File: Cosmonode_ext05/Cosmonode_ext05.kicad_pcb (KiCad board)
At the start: 2 copper layers, 25.4 x 34.3 mm, 16 parts, among them J1 CH340G, J2 GS2, J3 USB_OTG, J4 CONN_01X08, J5 CONN_01X08, J6 CONN_02X05, J7 CONN_01X09, Y1 Crystal_GND2

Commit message: big push!
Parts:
- added J8: Aloes_Logo, Aloes:Aloes_mini, F.Cu at (149.2, 119.4)
- C1, C2: footprint Capacitors_SMD:C_0402_NoSilk -> Capacitors_SMD:C_0603_HandSoldering
- J2: value GS2 -> OSWH_Logo; footprint Connectors:GS2 -> Symbols:OSHW-Logo_5.7x6mm_SilkScreen; moved to B.Cu
- R1, R2, R3, R4: footprint Resistors_SMD:R_0402_NoSilk -> Resistors_SMD:R_0603_HandSoldering
- moved J2 19.8 mm to (153.7, 102.2), turned to 270 degrees
- moved Y1 9.69 mm to (166.4, 109.2), turned to 90 degrees
- moved C1 4.49 mm to (165.7, 101.0), turned to 180 degrees
- moved R2 4.07 mm to (160.0, 104.1)
- moved J6 3.17 mm to (165.1, 118.1)
- moved C2 1.91 mm to (165.7, 104.1), turned to 180 degrees
- moved R1 1.91 mm to (160.0, 101.0)
- moved U1 1.42 mm to (158.8, 110.5)
- moved R3 0.64 mm to (154.3, 104.1), turned to 180 degrees
- moved R4 0.64 mm to (154.3, 101.0)
- moved J3 0.64 mm to (148.6, 110.5)
- renumbered J1 to U1
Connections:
- J7 pad 9: /DTR_1 -> /AREF
- U1 pad 13: /DTR_2 -> Net-(J1-Pad13)
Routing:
- net VCC: track 0.00 -> 69.2 mm
- net /RST: track 0.00 -> 27.1 mm
- net Net-(J1-Pad8): track 0.00 -> 22.7 mm
- net /RX: track 0.00 -> 20.5 mm, vias 0 -> 1
- net /MISO: track 0.00 -> 18.3 mm
- net /TX: track 0.00 -> 17.7 mm
- net Net-(J1-Pad7): track 0.00 -> 16.6 mm
- net /SCK: track 0.00 -> 14.8 mm
- net Net-(J3-Pad6): track 0.00 -> 13.2 mm
- net Net-(C1-Pad1): track 0.00 -> 12.1 mm, vias 0 -> 2
- net GND: track 0.00 -> 11.9 mm, vias 0 -> 6
- net /MOSI: track 0.00 -> 11.8 mm
- net Net-(J1-Pad2): track 0.00 -> 9.70 mm, vias 0 -> 2
- net /USB_N: track 0.00 -> 9.32 mm
- net /USB_P: track 0.00 -> 8.92 mm
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- added copper zone on B.Cu, net GND
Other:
- board text added: "ALOES.IO"

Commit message: big push2
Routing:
- added copper zone on F.Cu, net GND
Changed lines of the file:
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@@
     (links 43)
     (no_connects 0)
-    (area 144.165 85.565 192 130.763333)
+    (area 146.609999 93.904999 172.160001 128.345001)
     (thickness 1.6)
     (drawings 31)
@@
     (trace_clearance 0.2)
     (zone_clearance 0.508)
-    (zone_45_only no)
+    (zone_45_only yes)
     (trace_min 0.2)
     (segment_width 0.2)
@@
     (tags "Micro-USB SMD Typ-B")
     (attr smd)
-    (fp_text reference J3 (at 0 -4 270) (layer F.SilkS)
+    (fp_text reference J3 (at 0 -1.27 270) (layer F.SilkS)
       (effects (font (size 1 1) (thickness 0.15)))
     )
@@
     (fp_line (start 3.9 -0.8) (end 3.9 -2.65) (layer F.SilkS) (width 0.12))
     (fp_line (start 3.9 -2.65) (end 3.45 -2.65) (layer F.SilkS) (width 0.12))
-    (fp_text user %R (at 0 0 270) (layer F.Fab)
+    (fp_text user %R (at 0 0 270) (layer F.Fab) hide
       (effects (font (size 1 1) (thickness 0.15)))
     )
@@
     (descr "Through hole straight pin header, 2x05, 2.54mm pitch, double rows")
     (tags "Through hole pin header THT 2x05 2.54mm double row")
-    (fp_text reference J6 (at 1.27 -2.33 270) (layer F.SilkS)
+    (fp_text reference J6 (at 1.27 5.08 360) (layer F.SilkS)
       (effects (font (size 1 1) (thickness 0.15)))
     )
@@
     (at 166.37 109.22 90)
     (attr smd)
-    (fp_text reference Y1 (at -0.127 -1.7145 90) (layer F.SilkS)
+    (fp_text reference Y1 (at 0 1.905 90) (layer F.SilkS)
       (effects (font (size 1 1) (thickness 0.15)))
     )
@@
     (tags "resistor 0603")
     (attr smd)
-    (fp_text reference R2 (at 0 1.27) (layer F.SilkS)
+    (fp_text reference R2 (at 0 -1.27) (layer F.SilkS)
       (effects (font (size 1 1) (thickness 0.15)))
     )
@@
     (tags "resistor 0603")
     (attr smd)
-    (fp_text reference R3 (at 0 -1.45 180) (layer F.SilkS)
+    (fp_text reference R3 (at 0 1.27 180) (layer F.SilkS)
       (effects (font (size 1 1) (thickness 0.15)))
     )
@@
     (connect_pads (clearance 0.508))
     (min_thickness 0.254)
+    (fill yes (arc_segments 16) (thermal_gap 0.508) (thermal_bridge_width 0.508))
+    (polygon
+      (pts
+        (xy 172.085 97.155) (xy 172.085 125.73) (xy 169.545 128.27) (xy 146.685 128.27) (xy 146.685 93.98)
+        (xy 168.91 93.98)
+      )
+    )
+  )
+  (zone (net 2) (net_name GND) (layer F.Cu) (hatch edge 0.508)
+    (connect_pads (clearance 0.508))
+    (min_thickness 0.254)

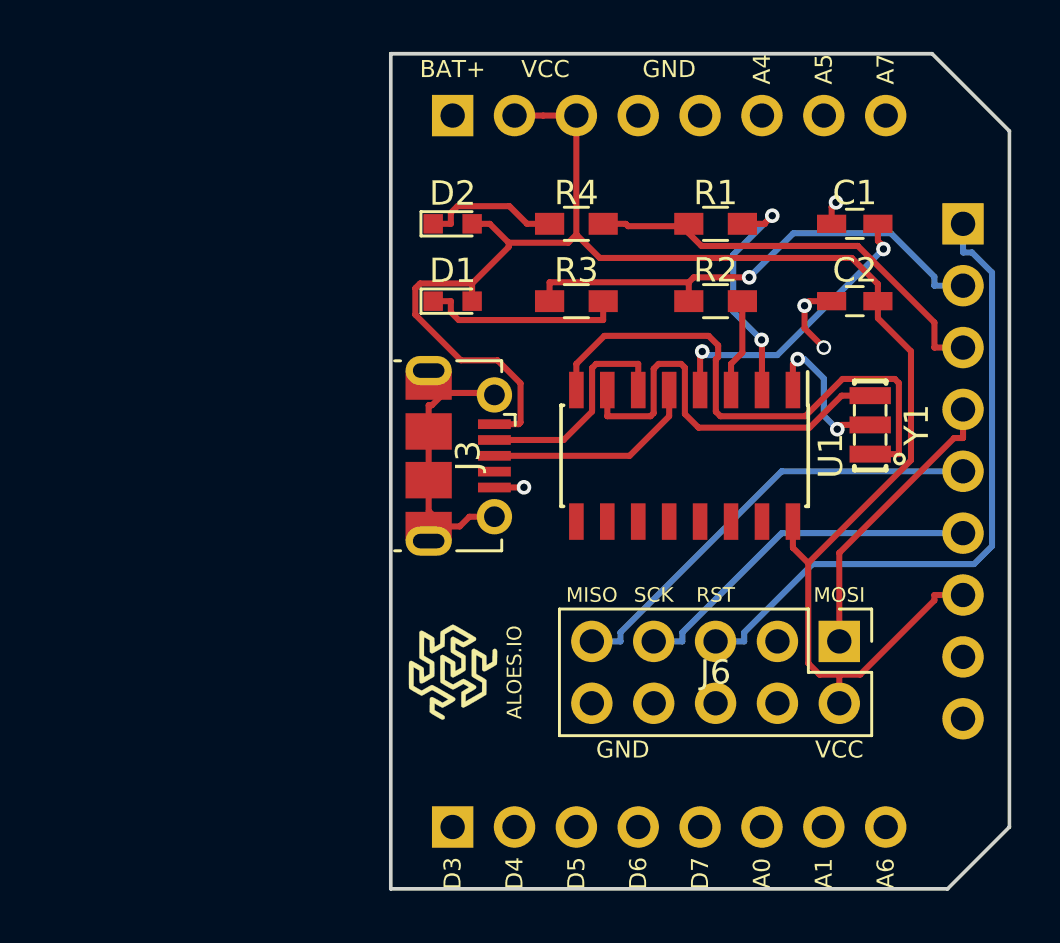
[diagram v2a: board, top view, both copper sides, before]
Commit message: update to v0.5 ( base, ext05, ext07, ext08 )
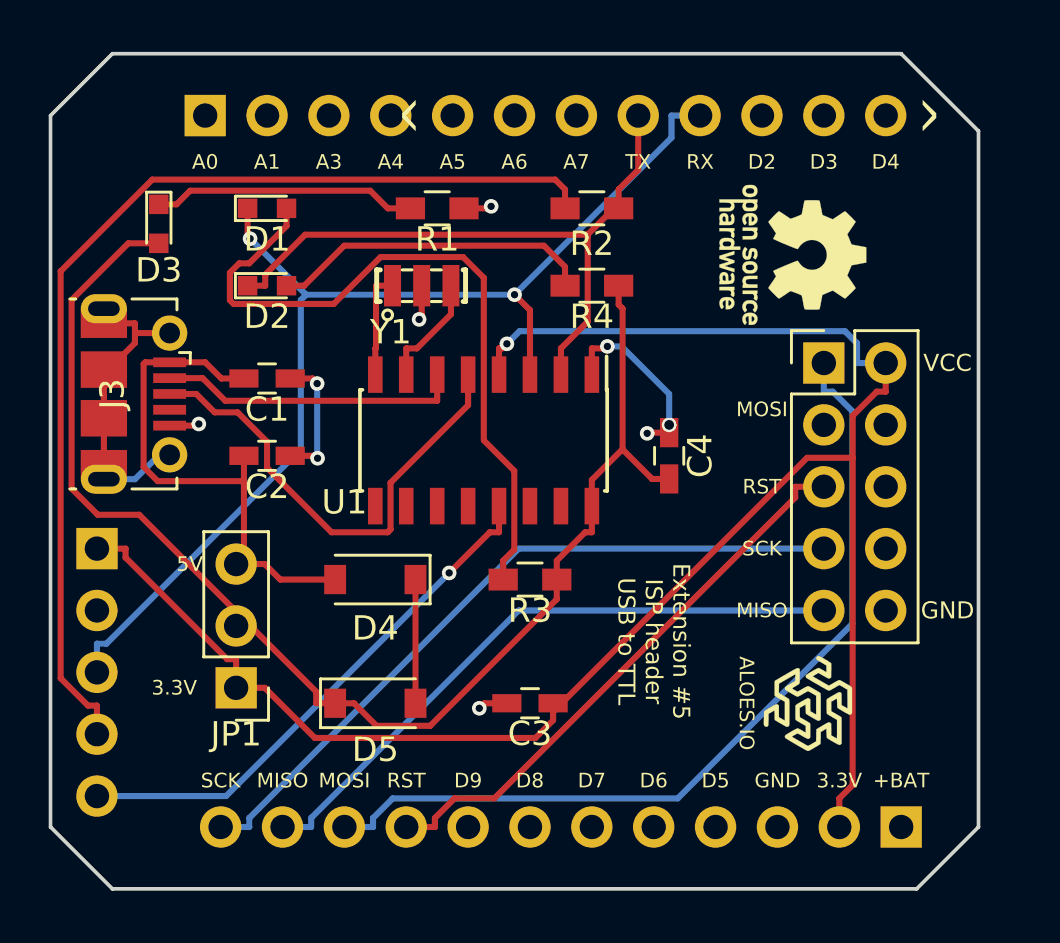
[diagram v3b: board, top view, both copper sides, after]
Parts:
- added C3: 100nF, Capacitors_SMD:C_0603_HandSoldering, F.Cu at (152.4, 120.7)
- added C4: 100nF, Capacitors_SMD:C_0603_HandSoldering, F.Cu at (158.1, 110.5)
- added D3: 0603, LEDs:LED_0603, F.Cu at (137.2, 101.0)
- added D4: MBR0520, Diodes_SMD:D_SOD-123, F.Cu at (146.1, 115.6)
- added D5: MBR0520, Diodes_SMD:D_SOD-123, F.Cu at (146.1, 120.7)
- added JP1: Jumper_NC_Dual, Pin_Headers:Pin_Header_Straight_1x03_Pitch2.54mm, F.Cu at (140.3, 120.0)
- C1: value 100nF -> 10uF
- J2: moved to F.Cu
- J4: value CONN_01X08 -> CONN_01X12; footprint Socket_Strips:Socket_Strip_Straight_1x08_Pitch2.54mm -> Socket_Strips:Socket_Strip_Straight_1x12_Pitch2.54mm
- J5: value CONN_01X08 -> CONN_01X05; footprint Socket_Strips:Socket_Strip_Straight_1x08_Pitch2.54mm -> Socket_Strips:Socket_Strip_Straight_1x05_Pitch2.54mm
- J7: value CONN_01X09 -> CONN_01X12; footprint Socket_Strips:Socket_Strip_Straight_1x09_Pitch2.54mm -> Socket_Strips:Socket_Strip_Straight_1x12_Pitch2.54mm
- R1: value 1k -> 1k5
- R2: value 1K -> 1k5
- R3, R4: value 5k -> 1k5
- Y1: value Crystal_GND2 -> CSTCE12M0V53-R0; footprint SMD-RESONATOR-8MHZ-33PF-0.1__3P-3.2X1.3MM_:X3-SMD-3.6X1.3X0.8MM -> SMD-RESONATOR-8MHZ-33PF:X3-SMD-3.6X1.3X0.8MM
- moved J4 34.5 mm to (167.6, 125.7), turned to 90 degrees
- moved J7 31.4 mm to (139.1, 96.5), turned to 270 degrees
- moved C1 25.0 mm to (141.6, 107.3), turned to 0 degrees
- moved C2 25.0 mm to (141.6, 110.5), turned to 0 degrees
- moved Y1 19.3 mm to (148.0, 103.5), turned to 0 degrees
- moved J5 18.5 mm to (134.6, 114.3), turned to 180 degrees
- moved J8 14.7 mm to (163.8, 120.7), turned to 270 degrees
- moved J3 13.6 mm to (135.3, 108.0)
- moved R3 11.6 mm to (152.4, 115.6), turned to 0 degrees
- moved R1 11.4 mm to (148.6, 100.3), turned to 180 degrees
- moved J6 11.4 mm to (164.5, 106.7), turned to 0 degrees
- moved J2 9.53 mm to (163.2, 102.2)
- moved D1 8.52 mm to (141.6, 100.3)
- moved U1 8.28 mm to (150.5, 109.9)
- moved D2 8.03 mm to (141.6, 103.5)
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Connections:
- net /A4 renamed D7
- net /A5 renamed D8
- net /A7 renamed D9
- net /BAT+ renamed +BATT
- C1 pad 1: Net-(C1-Pad1) -> +5V
- C2 pad 1: VCC -> +5V
- D1 pad 1: Net-(D1-Pad1) -> RX
- D1 pad 2: VCC -> Net-(D1-Pad2)
- D2 pad 1: Net-(D2-Pad1) -> TX
- D2 pad 2: VCC -> Net-(D2-Pad2)
- J3 pad 1: VCC -> +5V
- J4 pad 2: VCC -> +3V3
- J4 pad 3: VCC -> GND
- J4 pad 4: GND -> D5
- J4 pad 5: GND -> D6
- J5 pad 1: /D3 -> +3V3
- J5 pad 2: /D4 -> GND
- J5 pad 3: /D5 -> RX
- J5 pad 4: /D6 -> Net-(J5-Pad4)
- J5 pad 5: /D7 -> DTR
- J6 pad 1: /MOSI -> MOSI
- J6 pad 2: VCC -> +3V3
- J6 pad 5: /RST -> RST
- J6 pad 7: /SCK -> SCK
- J6 pad 9: /MISO -> MISO
- J7 pad 1: /RST -> A0
- J7 pad 2: /RX -> A1
- J7 pad 3: /TX -> A3
- J7 pad 4: /MOSI -> A4
- J7 pad 5: /MISO -> A5
- J7 pad 6: /SCK -> A6
- J7 pad 7: VCC -> A7
- J7 pad 8: GND -> TX
- J7 pad 9: /AREF -> RX
- R1 pad 1: /TX -> GND
- R1 pad 2: Net-(J1-Pad2) -> Net-(D3-Pad1)
- R2 pad 1: /RX -> TX
- R2 pad 2: Net-(J1-Pad3) -> Net-(J5-Pad4)
- R3 pad 1: Net-(D1-Pad1) -> Net-(D1-Pad2)
- R3 pad 2: /RX -> Net-(C4-Pad1)
- R4 pad 1: Net-(D2-Pad1) -> Net-(D2-Pad2)
- R4 pad 2: /TX -> Net-(C4-Pad1)
- U1 pad 13: Net-(J1-Pad13) -> DTR
- U1 pad 16: VCC -> Net-(C4-Pad1)
- U1 pad 2: Net-(J1-Pad2) -> TX
- U1 pad 3: Net-(J1-Pad3) -> RX
- U1 pad 4: Net-(C1-Pad1) -> +3V3
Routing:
- net +3V3: track 0.00 -> 78.8 mm, vias 0 -> 1
- net VCC: track 69.2 -> 0.00 mm
- net Net-(C4-Pad1): track 0.00 -> 55.9 mm
- net RX: track 0.00 -> 47.1 mm, vias 0 -> 2
- net Net-(J5-Pad4): track 0.00 -> 43.1 mm
- net MOSI: track 0.00 -> 35.9 mm
- net SCK: track 0.00 -> 29.7 mm
- net Net-(D1-Pad2): track 0.00 -> 29.7 mm
- net TX: track 0.00 -> 27.4 mm
- net /RST: track 27.1 -> 0.00 mm
- net MISO: track 0.00 -> 26.1 mm
- net RST: track 0.00 -> 23.4 mm
- net DTR: track 0.00 -> 22.1 mm, vias 0 -> 1
- net +5V: track 0.00 -> 21.9 mm
- net /RX: track 20.5 -> 0.00 mm, vias 1 -> 0
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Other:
- board size 25.4 x 34.3 mm -> 38.1 x 34.3 mm
- board text added: "+BAT"
- board text added: "3.3V"
- board text added: "5V"
- board text added: "A3"
- board text added: "D2"
- board text added: "D8"
- board text added: "D9"
- board text added: "RX"
- board text added: "TX"
- board text added: "^"
- board text removed: "BAT+"
